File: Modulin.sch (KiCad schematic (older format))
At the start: 21 parts

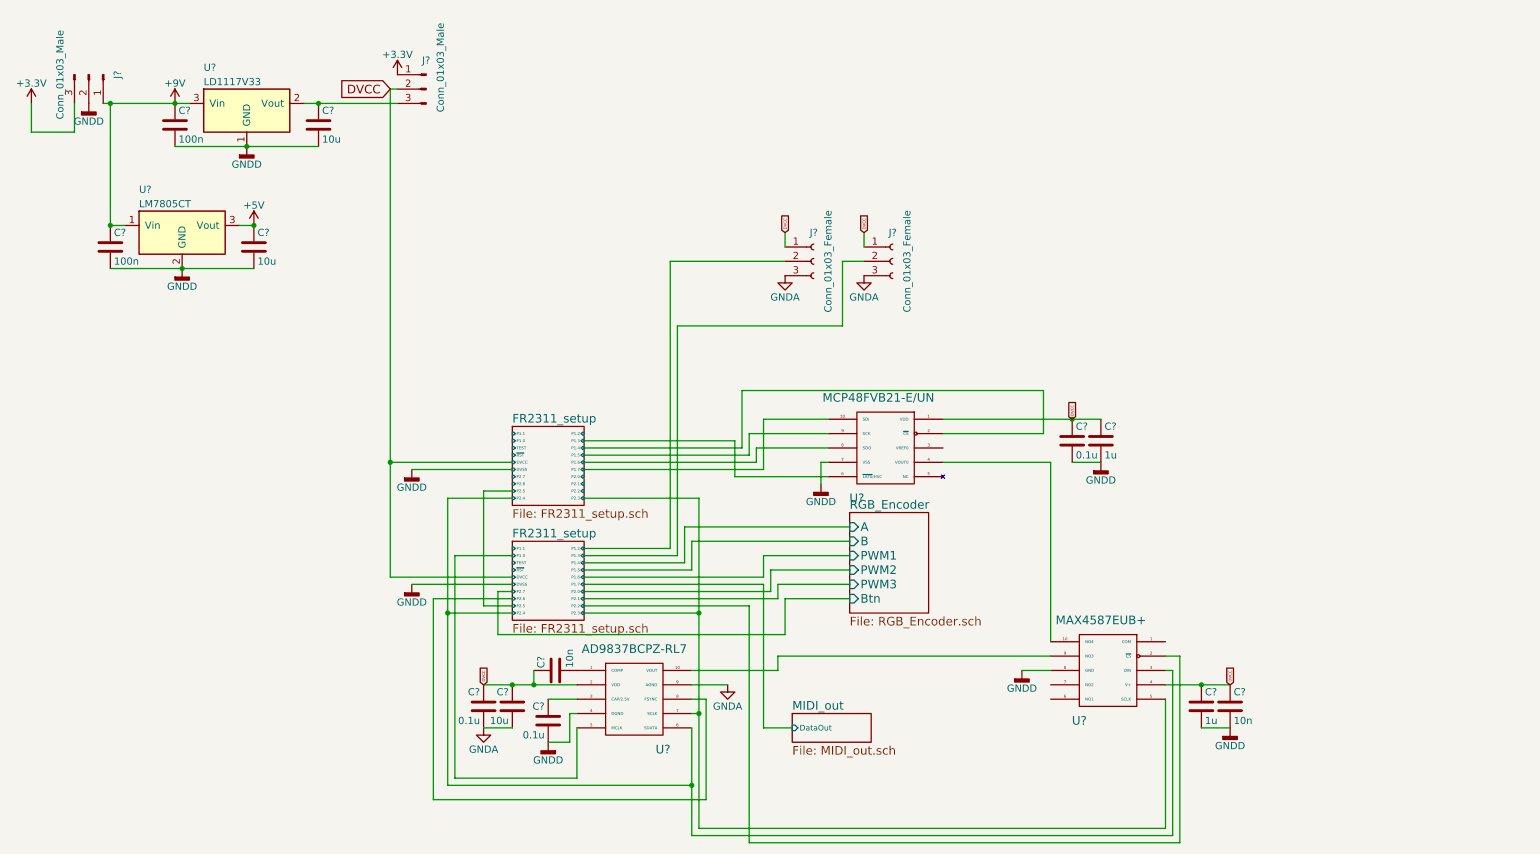
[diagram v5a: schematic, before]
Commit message: Finished Rev1 schematic and assigned most footprints
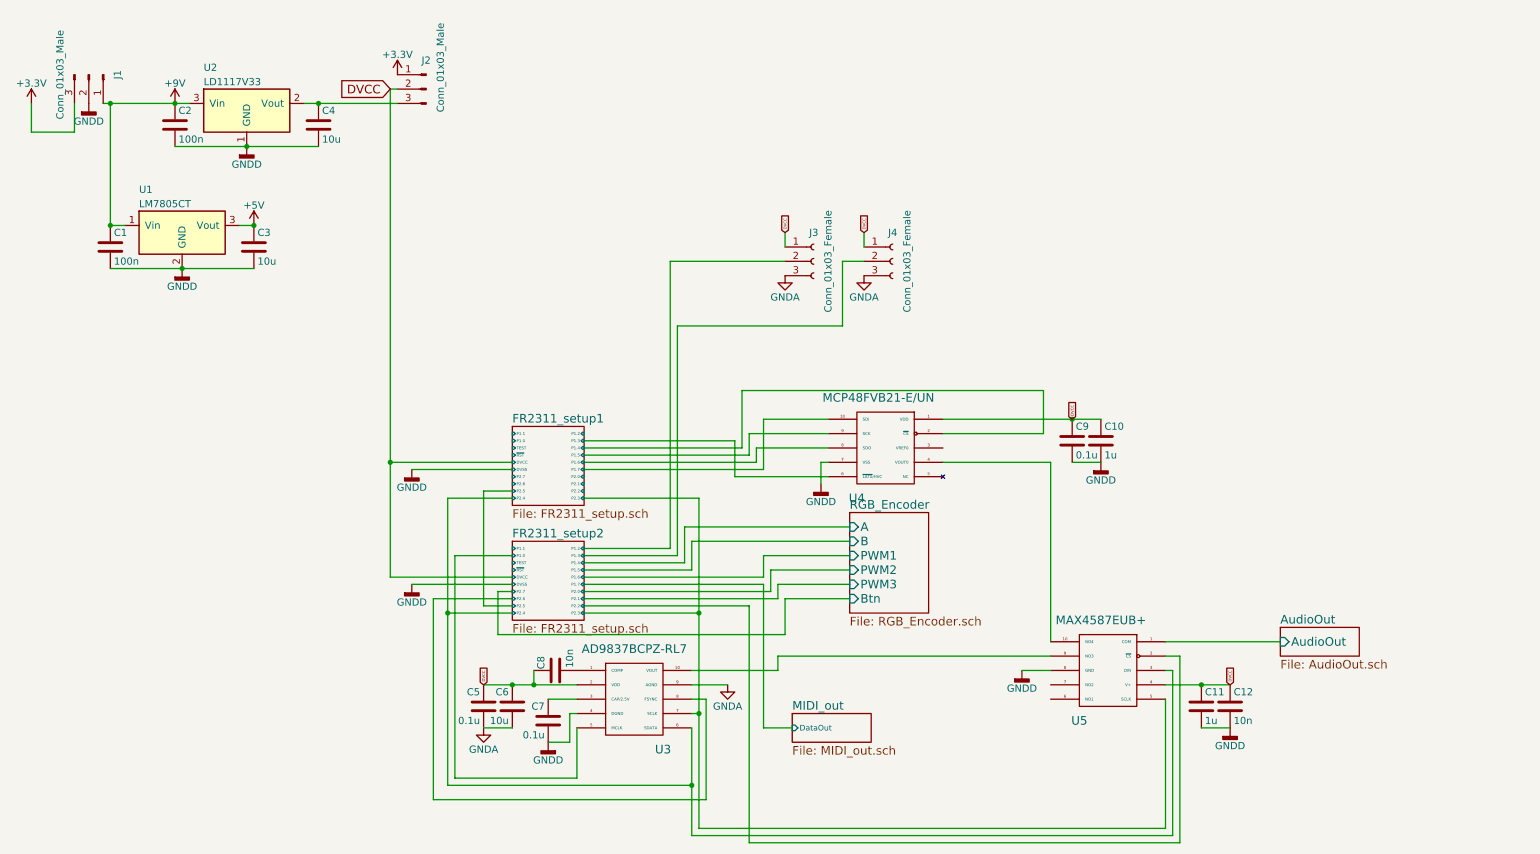
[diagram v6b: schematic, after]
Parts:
- C1, C10, C11, C12, C2, C3, C4, C5, C6, C7, C8, C9: renamed from C?; footprint (none) -> Capacitors_SMD:C_0603
- J1, J2, J3, J4: renamed from J?; footprint (none) -> Pin_Headers:Pin_Header_Angled_1x03_Pitch2.54mm
- U1: renamed from U?; footprint TO-220-3 -> TO_SOT_Packages_THT:TO-220-3_Horizontal
- U2: renamed from U?; footprint T-220-3 -> TO_SOT_Packages_THT:TO-220-3_Horizontal
- U4: renamed from U?; footprint (none) -> Housings_SSOP:MSOP-10_3x3mm_Pitch0.5mm
- gave numbers to parts that had none: 2
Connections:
- net AudioOut/AudioOut: now reaches U5.1 (COM)
- net FR2311_setup/P1.0 renamed FR2311_setup2/P1.0
- net FR2311_setup/P1.2 renamed FR2311_setup2/P1.2
- net FR2311_setup/P1.3 renamed FR2311_setup1/P1.3
- net FR2311_setup/P1.3 renamed FR2311_setup2/P1.3
- net FR2311_setup/P1.4 renamed FR2311_setup1/P1.4
- net FR2311_setup/P1.5 renamed FR2311_setup1/P1.5
- net FR2311_setup/P1.6 renamed FR2311_setup1/P1.6
- net FR2311_setup/P1.7 renamed FR2311_setup1/P1.7
- net FR2311_setup/P2.2 renamed FR2311_setup2/P2.2
- net FR2311_setup/P2.3 renamed FR2311_setup1/P2.3
- net FR2311_setup/P2.4 renamed FR2311_setup1/P2.4
- net FR2311_setup/P2.6 renamed FR2311_setup2/P2.6

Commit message: Associated all footprints except jacks
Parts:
- U3: footprint (none) -> Analog_Devices:AD9837BCPZ-RL7
- U5: footprint (none) -> Maxim_Integrated:MAX4587EUB&plus_
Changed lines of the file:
@@
 F 0 "U5" H 8300 4800 60  0000 C CNN
 F 1 "MAX4587EUB+" H 8150 5500 60  0000 C CNN
-F 2 "" H 8100 5100 60  0001 C CNN
+F 2 "Maxim_Integrated:MAX4587EUB&plus_" H 8100 5100 60  0001 C CNN
 F 3 "" H 8100 5100 60  0001 C CNN
 	1    8100 5100
@@
 F 0 "U3" H 5000 5000 60  0000 C CNN
 F 1 "AD9837BCPZ-RL7" H 4800 5700 60  0000 C CNN
-F 2 "" H 4800 5300 60  0001 C CNN
+F 2 "Analog_Devices:AD9837BCPZ-RL7" H 4800 5300 60  0001 C CNN
 F 3 "" H 4800 5300 60  0001 C CNN
 	1    4800 5300

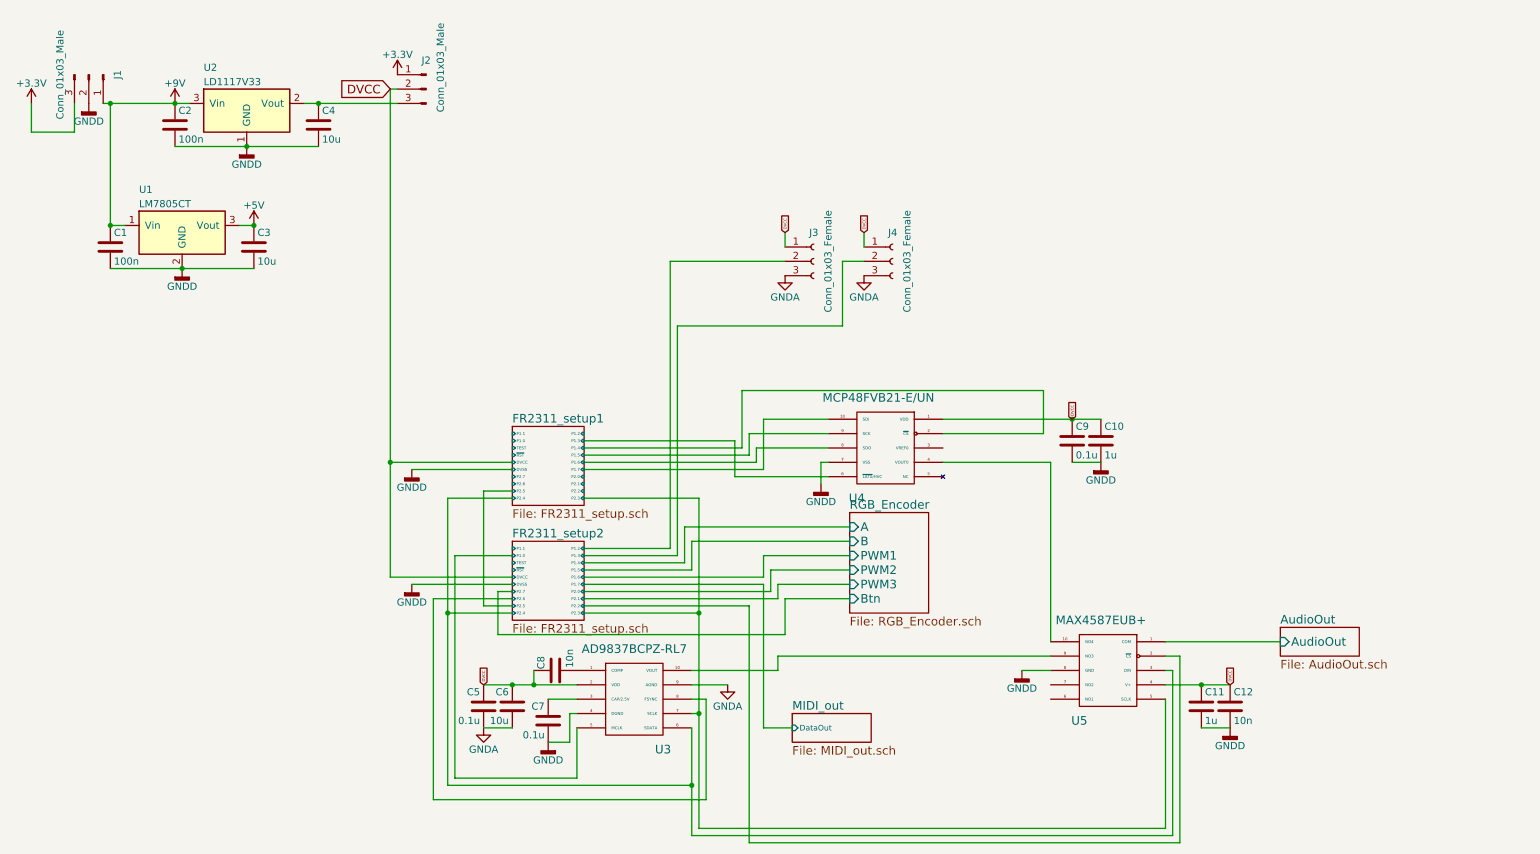
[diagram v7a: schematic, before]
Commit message: Halfway through layout. Started libraries.
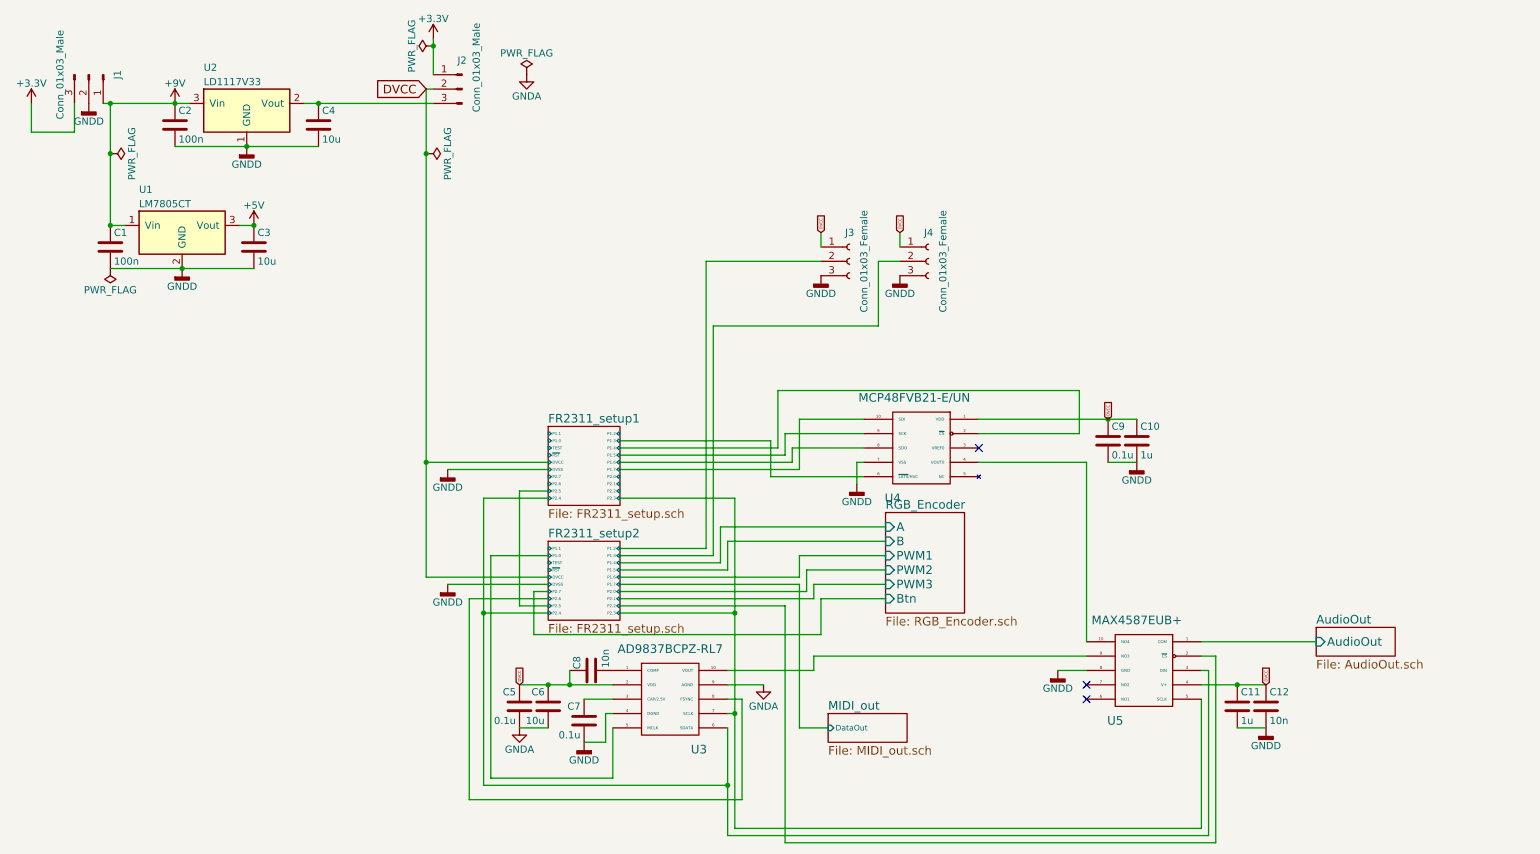
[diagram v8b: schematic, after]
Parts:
- J1, J2, J3, J4: footprint Pin_Headers:Pin_Header_Angled_1x03_Pitch2.54mm -> Pin_Headers:Pin_Header_Straight_1x03_Pitch2.54mm
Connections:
- net GNDA: no longer J3.3 (Pin_3), J4.3 (Pin_3)
- net GNDD: now also J3.3 (Pin_3), J4.3 (Pin_3)
- no-connect marks 0 -> 3
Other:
- moved on the sheet: C10, C11, C12, C5, C6, C7, C8, C9, J2, J3, J4, U3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
